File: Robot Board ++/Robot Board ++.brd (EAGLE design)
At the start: 68.6 x 76.2 mm, 127 parts, among them U10 74XX125.RGY, U11 SCHA4B0400, U12 BLUETOOTH-RN41", U13 XBEE-1XBEE-1_LOCK, U5 TPS5331[8/9].DQP, U6 TPS62082.DSG, U7 PCA9557.RGV, U8 MPU-6050, U9 ADS7830.PW

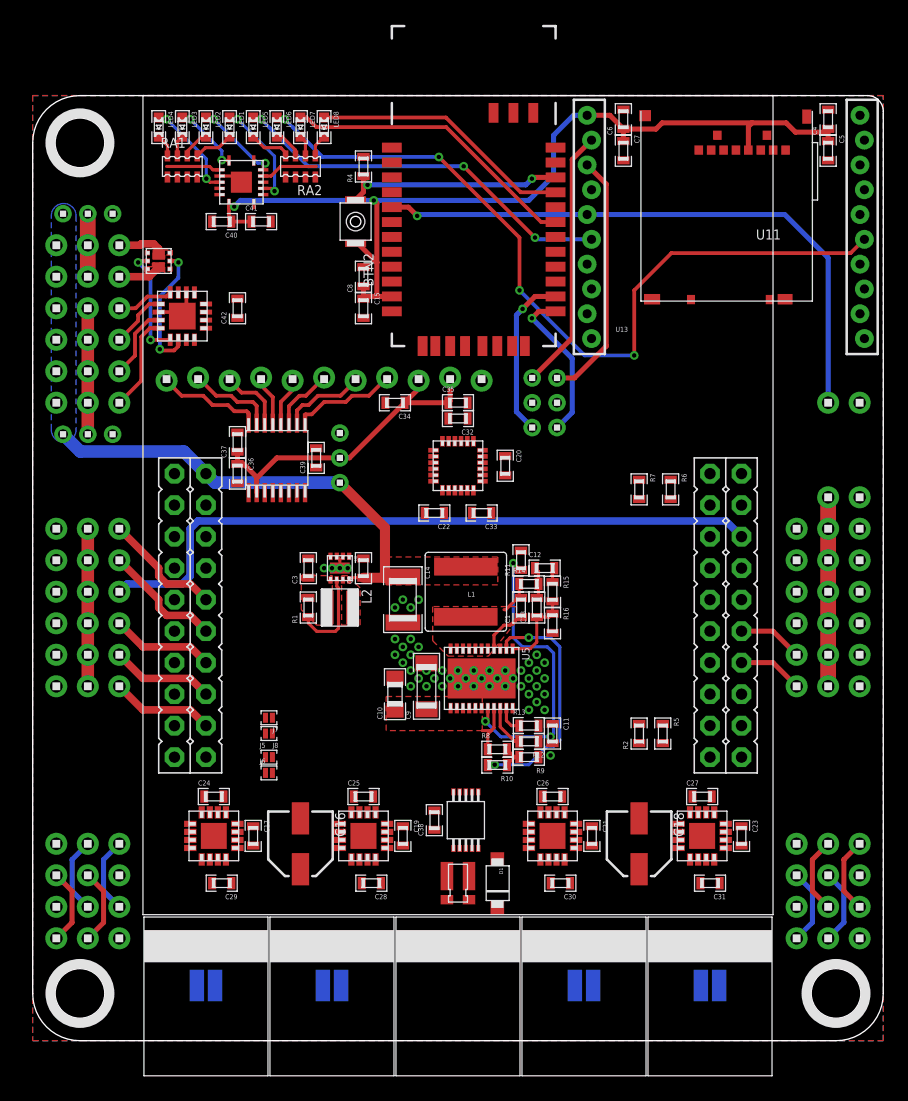
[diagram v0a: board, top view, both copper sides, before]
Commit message: Routing fun! Redrawing ratsnest is now taking a measurable amount of time...
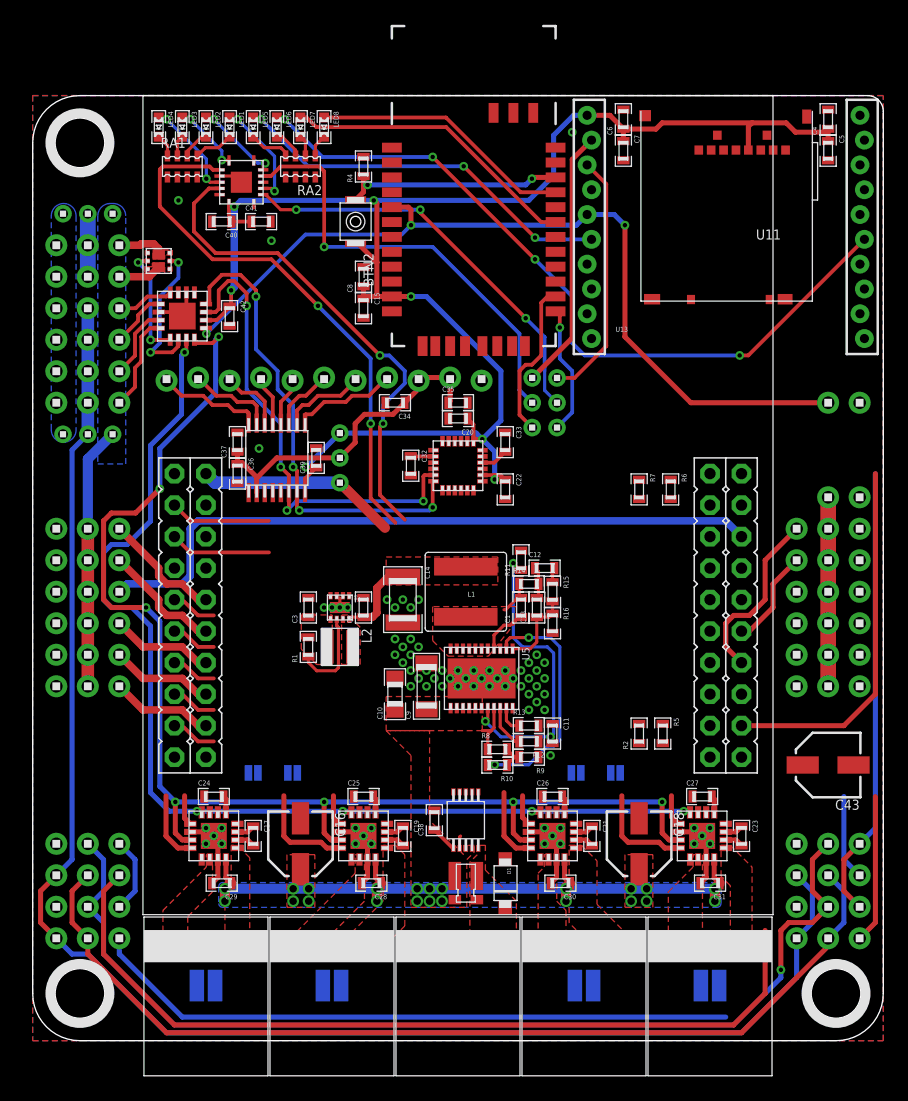
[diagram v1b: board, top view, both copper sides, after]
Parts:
- added C43: 100uF, microbuilder:PANASONIC_C
- J5, J6, J7, J8: device solderjumper:2.MED -> solderjumper:2.LRG
- moved J7 28.3 mm to (47.0, 21.6), flipped to the bottom
- moved J8 25.0 mm to (43.8, 21.6), flipped to the bottom
- moved H3 12.7 mm to (61.6, 41.3), turned to 270 degrees
- moved C22 6.02 mm to (38.1, 44.5), turned to 270 degrees
- moved C33 6.02 mm to (38.1, 48.3), turned to 270 degrees
- moved C20 5.39 mm to (34.3, 50.2), turned to 180 degrees
- moved C32 5.39 mm to (30.5, 46.4), turned to 270 degrees
- moved C2 3.18 mm to (26.7, 34.9)
- moved C3 3.18 mm to (22.2, 34.9)
- moved U6 3.18 mm to (24.8, 34.9)
- moved L2 3.17 mm to (24.8, 31.8)
- moved R1 3.17 mm to (22.2, 31.8)
- moved J6 1.90 mm to (21.0, 21.6), flipped to the bottom
- moved J5 1.80 mm to (17.8, 21.6), flipped to the bottom, turned to 180 degrees
- moved C42 0.90 mm to (15.9, 58.4), turned to 270 degrees
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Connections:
- removed net I2C.SDL: U9.14
- net 5.0V: now also C43.+
- net GND: now also C43.-
- net I2C.SCL: now also U9.14
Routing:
- net VDDIO: track 22.4 -> 126.9 mm
- net M.EN: track 0.00 -> 104.0 mm, vias 0 -> 7
- net M.MODE: track 0.00 -> 88.6 mm, vias 0 -> 5
- net SPI.MISO: track 12.3 -> 83.6 mm, vias 0 -> 1
- net ENC0.!CS: track 0.00 -> 68.7 mm
- net SPI.SCLK: track 12.3 -> 79.4 mm
- net 3.3V: track 88.1 -> 154.4 mm, vias 2 -> 7
- net SVRO4/ENC2.!CS: track 0.00 -> 56.0 mm
- net VBAT: track 4.25 -> 58.6 mm, vias 0 -> 22
- net 3.3V.PG: track 7.24 -> 47.4 mm, vias 0 -> 2
- net 5V.PG: track 4.39 -> 44.2 mm, vias 0 -> 2
- net UART.RXI: track 4.60 -> 44.3 mm, vias 0 -> 1
- net I2C.SCL: track 0.00 -> 38.8 mm, vias 0 -> 4
- net I2C.SDA: track 0.00 -> 38.3 mm, vias 0 -> 4
- net SPI.MOSI: track 12.3 -> 46.3 mm
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- added copper zone on layer 1, net M0+
- added copper zone on layer 1, net M0-
- added copper zone on layer 1, net M1+
- added copper zone on layer 1, net M1-
- added copper zone on layer 1, net M2+
- added copper zone on layer 1, net M2-
- added copper zone on layer 1, net M3+
- added copper zone on layer 1, net M3-
- added copper zone on layer 1, net N$22
- added copper zone on layer 16, net VBAT

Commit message: Added I2C and UART headers Connected most signals on PCB  Will need to clean up...
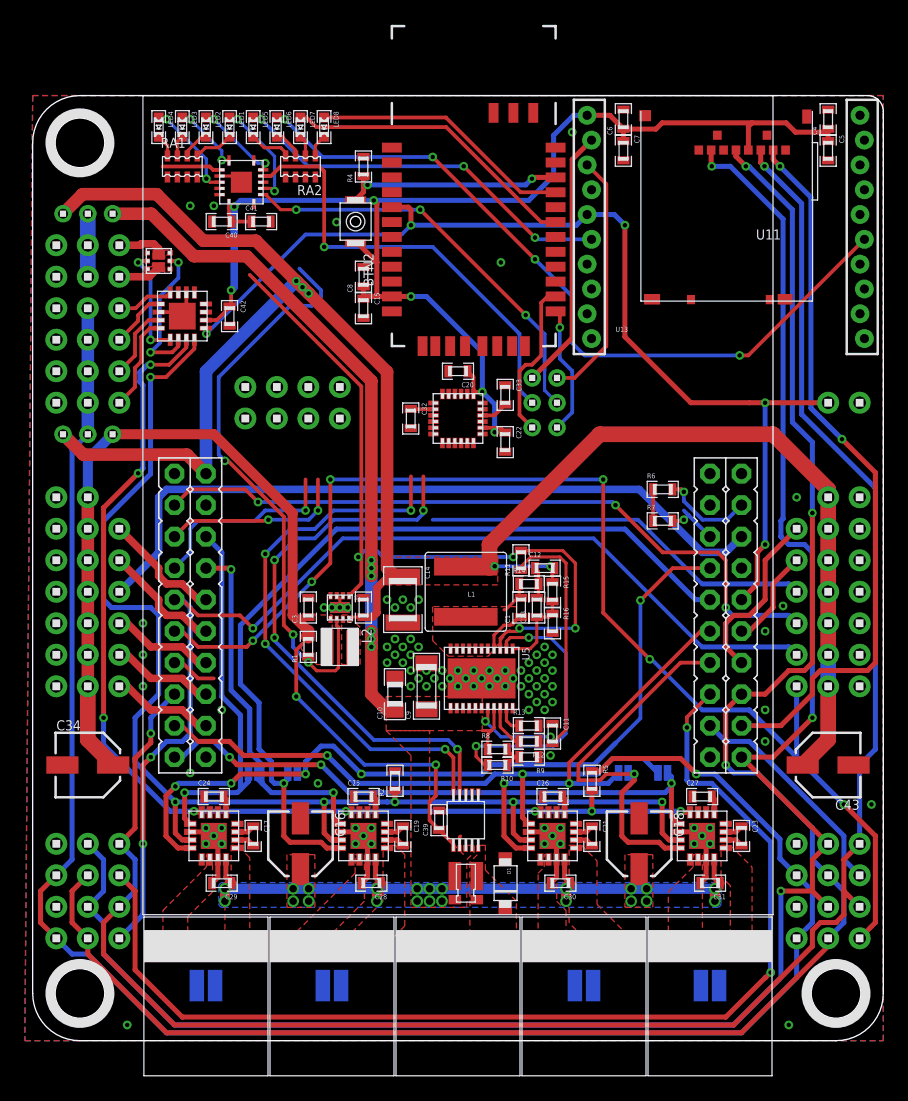
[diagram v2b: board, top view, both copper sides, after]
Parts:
- removed C35, C37: 1uF, standardparts:0603
- removed C36, C38: .1uF, standardparts:0603
- removed H28: 1X11.LOCK, headers(.1in):1X11.LOCK
- removed U9: ADS7830.PW, packages(ti):PW.16
- added U$6, U$7: 1X4, headers(.1in):1X4
- C34: value .1uF -> 100uF; device standardparts:0603 -> microbuilder:PANASONIC_C
- H26: value 1X3 -> 1X2; device headers(2mm):1X3 -> headers(.1in):1X2
- moved C34 38.3 mm to (4.45, 22.2), turned to 0 degrees
- moved C39 30.8 mm to (32.8, 17.8)
- moved H26 20.6 mm to (4.45, 43.8), turned to 180 degrees
- moved R2 20.1 mm to (29.2, 21.0)
- moved R5 6.87 mm to (45.1, 21.0)
- moved C20 3.81 mm to (34.3, 54.0)
- moved C32 3.81 mm to (30.5, 50.2)
- moved C33 3.81 mm to (38.1, 52.1)
- moved J8 3.81 mm to (47.6, 21.6)
- moved U8 3.81 mm to (34.3, 50.2)
- moved C22 3.81 mm to (38.1, 48.3)
- moved J7 3.81 mm to (50.8, 21.6)
- moved R7 3.18 mm to (50.8, 41.9), turned to 0 degrees
- moved R6 0.64 mm to (50.8, 44.5), turned to 0 degrees
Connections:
- removed net LS.1: H28.8, U9.1
- removed net LS.2: H28.7, U9.2
- removed net LS.3: H28.6, U9.3
- removed net LS.4: H28.5, U9.4
- removed net LS.5: H28.4, U9.5
- removed net LS.6: H28.3, U9.6
- removed net LS.7: H28.2, U9.7
- removed net LS.8: H28.1, U9.8
- removed net VCC: C34.1, C35.1, C36.1, C37.1, H26.2, H28.10, H28.9, U9.10
- net 3.3V: now also C34.+, U$6.1, U$7.1; no longer C38.1, U9.16
- net 5.0V: no longer H26.3
- net GND: now also C34.-, H26.2, U$6.4, U$7.4; no longer C34.2, C35.2, C36.2, C37.2, C38.2, H28.11, U9.11, U9.12, U9.13, U9.9
- net I2C.SCL: now also U$6.3; no longer U9.14
- net I2C.SDA: now also U$6.2; no longer U9.15
- net UART.RXI: now also U$7.3
- net UART.TXO: now also U$7.2
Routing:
- net 5.0V: track 39.7 -> 153.6 mm, vias 0 -> 5
- net SPI.MOSI: track 46.3 -> 159.2 mm, vias 0 -> 2
- net SVRO5/ENC3.!CS: track 15.7 -> 99.3 mm, vias 0 -> 6
- net SPI.SCLK: track 79.4 -> 149.8 mm, vias 0 -> 3
- net SPI.MISO: track 83.6 -> 152.5 mm, vias 1 -> 3
- net M0.DIR: track 5.60 -> 66.2 mm, vias 0 -> 5
- net M1.DIR: track 8.17 -> 68.2 mm, vias 0 -> 1
- net VBAT: track 58.6 -> 114.6 mm, vias 22 -> 28
- net SVRO3: track 8.15 -> 57.4 mm, vias 0 -> 3
- net M3.SPD: track 2.50 -> 47.2 mm, vias 0 -> 3
- net M2.SPD: track 6.18 -> 46.5 mm, vias 0 -> 2
- net 3.3V: track 154.4 -> 191.5 mm, vias 7 -> 8
- net SVRO4/ENC2.!CS: track 56.0 -> 89.3 mm, vias 0 -> 3
- net SVRO2: track 3.70 -> 35.5 mm
- net SPI.FSS: track 29.6 -> 58.4 mm, vias 0 -> 2
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- removed copper zone on layer 16, net 5.0V
